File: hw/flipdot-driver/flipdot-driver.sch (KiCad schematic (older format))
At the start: 7 parts

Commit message: Last version before 74HC595.
Only partially routed.
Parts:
- removed D?: D_ALT, symbol Device:D_ALT
- removed Q?: Q_PMOS_GSD, symbol Device:Q_PMOS_GSD
- removed R?: R, symbol Device:R
- removed U?: STM32F103C8Tx, Package_QFP:LQFP-48_7x7mm_P0.5mm, symbol MCU_ST_STM32F1:STM32F103C8Tx
- removed U?: ULN2803A, symbol Transistor_Array:ULN2803A
- added C1: 100u, Capacitor_SMD:CP_Elec_6.3x5.3, symbol controller-cache:CP
- added C10: 10n, Capacitor_SMD:C_0603_1608Metric, symbol controller-cache:C
- added C11: 22u, Capacitor_SMD:C_0805_2012Metric, symbol controller-cache:C
- added C12, C13: 10p, Capacitor_SMD:C_0603_1608Metric, symbol controller-cache:C
- added C14, C15: 27p, Capacitor_SMD:C_0603_1608Metric, symbol controller-cache:C
- added C2, C3: 1u, Capacitor_SMD:C_0603_1608Metric, symbol controller-cache:C
- added C4: 220u, Capacitor_SMD:CP_Elec_10x10, symbol controller-cache:CP
- added C5, C6, C7, C8: 100n, Capacitor_SMD:C_0603_1608Metric, symbol controller-cache:C
- added C9: 10u, Capacitor_SMD:C_0805_2012Metric, symbol controller-cache:C
- added D1, D6: SK33, Diode_SMD:D_SMC, symbol controller-cache:D_Schottky
- added D3, D4, D5: LED, LED_THT:LED_D5.0mm_Horizontal_O6.35mm_Z9.0mm, symbol controller-cache:LED
- added DC1: XL6009, Package_TO_SOT_SMD:TO-263-5_TabPin3, symbol controller-cache:XL6009
- added F1: 200mA, Fuse:Fuse_1206_3216Metric, symbol Device:Polyfuse
- added F2: Polyfuse, Fuse:Fuse_1812_4532Metric, symbol Device:Polyfuse
- added J10: AUX_Power, Connector_Molex:Molex_KK-254_AE-6410-02A_1x02_P2.54mm_Vertical, symbol Connector_Generic:Conn_01x02
- added J11: GND, user:TestPoint_Plated_Hole_D1.6mm, symbol Connector:Conn_01x01_Female
- added J12: +VIN, user:TestPoint_Plated_Hole_D1.6mm, symbol Connector:Conn_01x01_Female
- added J2: NRF_CON, Connector_PinSocket_2.54mm:PinSocket_2x04_P2.54mm_Vertical, symbol Connector_Generic:Conn_02x04_Odd_Even
- added J3: Prog, Connector_Molex:Molex_KK-254_AE-6410-05A_1x05_P2.54mm_Vertical, symbol Connector_Generic:Conn_01x05
- added J4: I2C, Connector_Molex:Molex_KK-254_AE-6410-04A_1x04_P2.54mm_Vertical, symbol Connector_Generic:Conn_01x04
- added J5: USART, Connector_Molex:Molex_KK-254_AE-6410-05A_1x05_P2.54mm_Vertical, symbol Connector_Generic:Conn_01x05
- added J6: USB, Connector_Molex:Molex_KK-254_AE-6410-04A_1x04_P2.54mm_Vertical, symbol Connector_Generic:Conn_01x04
- added J7: USB_B_Micro, symbol Connector:USB_B_Micro
- added J8: RST, Connector_PinSocket_2.54mm:PinSocket_1x02_P2.54mm_Vertical, symbol Connector_Generic:Conn_01x02
- added J9: MAIN_Power, Connectors_Phoenix:PhoenixContact_MC-G_02x3.81mm_Angled, symbol Connector_Generic:Conn_01x02
- added L1: 33u, Inductor_SMD:L_12x12mm_H8mm, symbol controller-cache:L
- added Q1, Q10, Q11, Q12, Q13, Q14, Q2, Q3, Q4, Q5, Q6, Q7, Q8, Q9: MMBTA64, dboard_footprints:SOT23-3, symbol Device:Q_PNP_Darlington_BEC
- added Q15, Q16, Q17, Q18: Q_NMOS_GSD, Package_TO_SOT_SMD:SOT-23, symbol Device:Q_NMOS_GSD
- added R1, R13, R16, R27, R28, R29, R30, R31, R32, R33, R34: 12k, Resistor_SMD:R_0603_1608Metric, symbol Device:R
- added R14, R15: 22R, Resistor_SMD:R_0603_1608Metric, symbol Device:R
- added R2: 680R, Resistor_SMD:R_0603_1608Metric, symbol Device:R
- added R24: 1k5, Resistor_SMD:R_0603_1608Metric, symbol Device:R
- added R25, R3, R4: 330R, Resistor_SMD:R_0603_1608Metric, symbol Device:R
- added R26: 4k7, Resistor_SMD:R_0603_1608Metric, symbol Device:R
- added R35: 1M, Resistor_SMD:R_0603_1608Metric, symbol Device:R
- added R36: 1k5, Resistor_SMD:R_0603_1608Metric, symbol controller-cache:R
- added RN1, RN2, RN3, RN4: 10k, Resistor_SMD:R_Array_Convex_4x0603, symbol Device:R_Pack04
- added TP1: TestPoint, TestPoint:TestPoint_THTPad_2.5x2.5mm_Drill1.2mm, symbol Connector:TestPoint
- added U1: AT25xxx, Package_SO:SO-8_5.3x6.2mm_P1.27mm, symbol Memory_EEPROM:AT25xxx
- added U3: USBLC6-2SC6, Package_TO_SOT_SMD:SOT-23-6, symbol Power_Protection:USBLC6-2SC6
- added U4: AZ1117-3.3, Package_TO_SOT_SMD:SOT-223-3_TabPin2, symbol Regulator_Linear:AZ1117-3.3
- added U5: ULN2003A, Package_SO:SOIC-16_3.9x9.9mm_P1.27mm, symbol Transistor_Array:ULN2003A
- added U6: stm32_STM32F103C(8-B)Tx, Package_QFP:LQFP-48_7x7mm_P0.5mm, symbol STM32_converter-cache:stm32_STM32F103C(8-B)Tx
- added Y1: 32768, Crystal:Crystal_Round_D3.0mm_Vertical, symbol Device:Crystal
- added Y2: 8MHz/20pF, Crystal:Crystal_HC49-U_Vertical, symbol Device:Crystal
- J1: renamed from J?; value Conn_02x10_Top_Bottom -> DISPLAY; footprint (none) -> Connector_IDC:IDC-Header_2x10_P2.54mm_Vertical
- U2: renamed from U?; footprint (none) -> Package_SO:SOIC-16_3.9x9.9mm_P1.27mm
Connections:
- net labels added: +12V, +3V3, 24V_EN, FLASH_SS, I2C_SCL, I2C_SDA, LV_CLK, LV_DATA, LV_R1N, LV_R1P, LV_R2N, LV_R2P, LV_R3N, LV_R3P, LV_R4N, LV_R4P, LV_R5N, LV_R5P, LV_R6N, LV_R6P, LV_R7N, LV_R7P, LV_RET, LV_RST, NRF_CE, NRF_IRQ, NRF_SS, NRST, SPI_MISO, SPI_MOSI, SPI_SCK, SWCLK, SWDIO, USART_RX, USART_TX, USB1_N, USB1_P, USB_N, USB_P
- wire segments 28 -> 436
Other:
- moved on the sheet: J1, U2

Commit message: Added 74HC595 and AX5201
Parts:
- added C16: 470u, Capacitor_SMD:CP_Elec_6.3x5.3, symbol flipdot-driver-rescue:CP-controller-cache
- added C17: 100n, Capacitor_SMD:C_0603_1608Metric, symbol flipdot-driver-rescue:C-controller-cache
- added C18, C19: 470n, Capacitor_SMD:C_0603_1608Metric, symbol flipdot-driver-rescue:C-controller-cache
- added C20: 1u, Capacitor_SMD:C_0603_1608Metric, symbol flipdot-driver-rescue:C-controller-cache
- added C21: 220u, Capacitor_SMD:CP_Elec_10x10, symbol flipdot-driver-rescue:CP-controller-cache
- added D2: SK34, Diode_SMD:D_SMC, symbol flipdot-driver-rescue:D_Schottky-controller-cache
- added D7, D8: LED, LED_THT:LED_D5.0mm, symbol flipdot-driver-rescue:LED-controller-cache
- added L2: 68u, Inductor_SMD:L_12x12mm_H8mm, symbol flipdot-driver-rescue:L-controller-cache
- added R10, R5: 12k, Resistor_SMD:R_0603_1608Metric, symbol Device:R
- added R6: 30k, Resistor_SMD:R_0603_1608Metric, symbol Device:R
- added R7: 1.3k, Resistor_SMD:R_0603_1608Metric, symbol Device:R
- added R8, R9: 330R, Resistor_SMD:R_0603_1608Metric, symbol Device:R
- added TP2: TestPoint, TestPoint:TestPoint_THTPad_2.5x2.5mm_Drill1.2mm, symbol Connector:TestPoint
- added U7, U9: 74HC595, Package_SO:SOIC-16_3.9x9.9mm_P1.27mm, symbol 74xx:74HC595
- added U8: AX5201, Package_SO:HSOP-8-1EP_3.9x4.9mm_P1.27mm_EP2.41x3.1mm, symbol LCSC:AX5201
- C1, C4: symbol controller-cache:CP -> flipdot-driver-rescue:CP-controller-cache
- C10, C11, C12, C13, C14, C15, C2, C3, C5, C6, C7, C8, C9: symbol controller-cache:C -> flipdot-driver-rescue:C-controller-cache
- D1, D6: symbol controller-cache:D_Schottky -> flipdot-driver-rescue:D_Schottky-controller-cache
- D3, D4, D5: footprint LED_THT:LED_D5.0mm_Horizontal_O6.35mm_Z9.0mm -> LED_THT:LED_D5.0mm; symbol controller-cache:LED -> flipdot-driver-rescue:LED-controller-cache
- DC1: symbol controller-cache:XL6009 -> flipdot-driver-rescue:XL6009-controller-cache
- L1: symbol controller-cache:L -> flipdot-driver-rescue:L-controller-cache
- R36: symbol controller-cache:R -> flipdot-driver-rescue:R-controller-cache
- U6: symbol STM32_converter-cache:stm32_STM32F103C(8-B)Tx -> flipdot-driver-rescue:stm32_STM32F103C(8-B)Tx-STM32_converter-cache
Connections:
- net labels added: BOOT1, LED1, LED2, LV_RES, SR_CLK, SR_DATA1, SR_DATA2, SR_STROBE, ~SR_OE
- net labels removed: LV_R1N, LV_R1P, LV_R2N, LV_R2P, LV_R3N, LV_R3P, LV_R4N, LV_R4P, LV_R5N, LV_R5P, LV_R6N, LV_R6P, LV_R7N, LV_R7P
- wire segments 436 -> 521
- no-connect marks 0 -> 3
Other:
- moved on the sheet: F1, J1, J2, J3, J4, J5, Q1, Q2, Q3, Q4, Q5, Q6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

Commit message: Routed, with unused parts.
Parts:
- removed R14, R15: 22R, Resistor_SMD:R_0603_1608Metric, symbol Device:R
- added C22: 100n, Capacitor_SMD:C_0603_1608Metric, symbol flipdot-driver-rescue:C-controller-cache-flipdot-driver-rescue
- added R11, R12: 1k5, Resistor_SMD:R_0603_1608Metric, symbol controller-cache:R
- added RN5: 22R, Resistor_SMD:R_Array_Convex_2x0402, symbol Device:R_Pack02
- C1, C16, C4: symbol flipdot-driver-rescue:CP-controller-cache -> flipdot-driver-rescue:CP-controller-cache-flipdot-driver-rescue
- C10, C11, C12, C13, C14, C15, C17, C18, C19, C2, C20, C3, C5, C6, C7, C8, C9: symbol flipdot-driver-rescue:C-controller-cache -> flipdot-driver-rescue:C-controller-cache-flipdot-driver-rescue
- C21: value 220u -> 470u; symbol flipdot-driver-rescue:CP-controller-cache -> flipdot-driver-rescue:CP-controller-cache-flipdot-driver-rescue
- D1, D2, D6: symbol flipdot-driver-rescue:D_Schottky-controller-cache -> flipdot-driver-rescue:D_Schottky-controller-cache-flipdot-driver-rescue
- D3, D4, D5, D7, D8: footprint LED_THT:LED_D5.0mm -> LED_THT:LED_D3.0mm; symbol flipdot-driver-rescue:LED-controller-cache -> flipdot-driver-rescue:LED-controller-cache-flipdot-driver-rescue
- DC1: symbol flipdot-driver-rescue:XL6009-controller-cache -> flipdot-driver-rescue:XL6009-controller-cache-flipdot-driver-rescue
- J7: footprint (none) -> stm32_converter_footprints:USB_Micro-B
- L1, L2: symbol flipdot-driver-rescue:L-controller-cache -> flipdot-driver-rescue:L-controller-cache-flipdot-driver-rescue
- R36: symbol flipdot-driver-rescue:R-controller-cache -> flipdot-driver-rescue:R-controller-cache-flipdot-driver-rescue
- U6: symbol flipdot-driver-rescue:stm32_STM32F103C(8-B)Tx-STM32_converter-cache -> flipdot-driver-rescue:stm32_STM32F103C(8-B)Tx-STM32_converter-cache-flipdot-driver-rescue
- U8: symbol LCSC:AX5201 -> flipdot-driver-rescue:AX5201-LCSC
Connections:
- net labels added: USB2_N, USB2_P
- net labels removed: LV_RES
- wire segments 521 -> 529
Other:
- moved on the sheet: J4

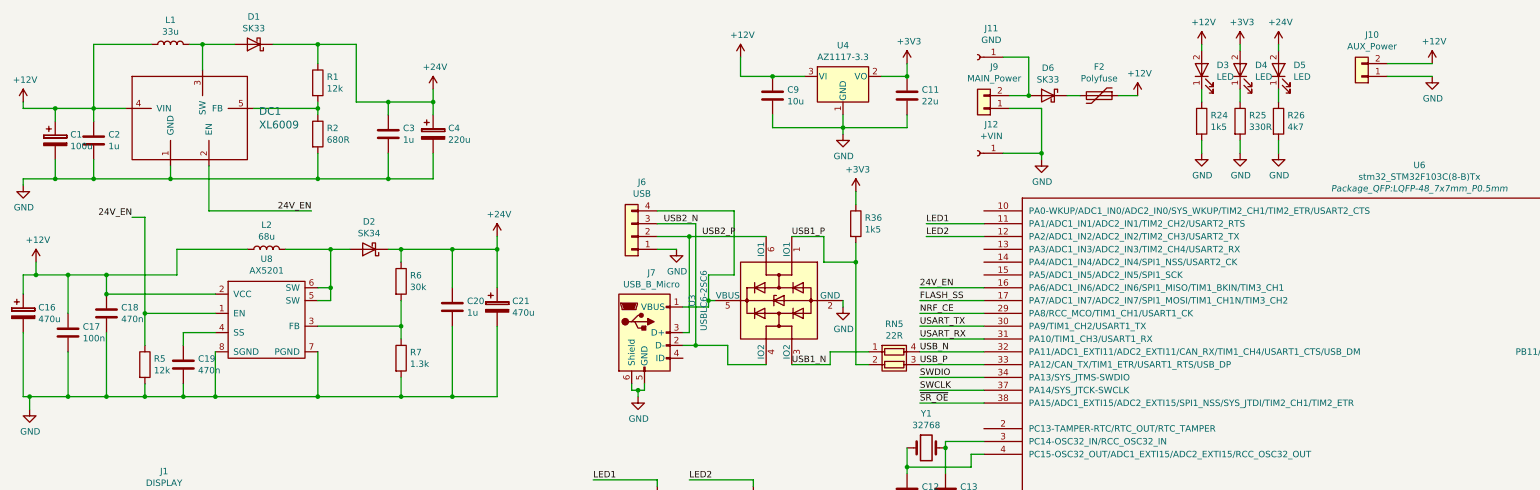
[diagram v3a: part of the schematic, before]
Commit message: Routed, without unused parts.
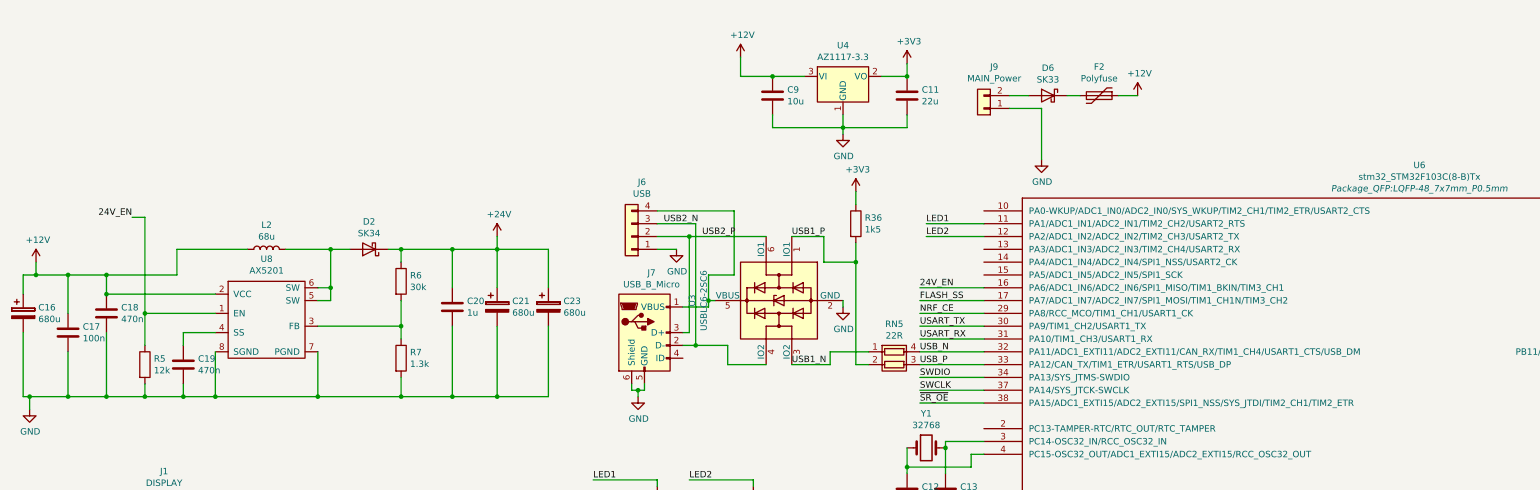
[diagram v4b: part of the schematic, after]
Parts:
- removed C1: 100u, Capacitor_SMD:CP_Elec_6.3x5.3, symbol flipdot-driver-rescue:CP-controller-cache-flipdot-driver-rescue
- removed C2, C3: 1u, Capacitor_SMD:C_0603_1608Metric, symbol flipdot-driver-rescue:C-controller-cache-flipdot-driver-rescue
- removed C4: 220u, Capacitor_SMD:CP_Elec_10x10, symbol flipdot-driver-rescue:CP-controller-cache-flipdot-driver-rescue
- removed D1: SK33, Diode_SMD:D_SMC, symbol flipdot-driver-rescue:D_Schottky-controller-cache-flipdot-driver-rescue
- removed D3, D4, D5: LED, LED_THT:LED_D3.0mm, symbol flipdot-driver-rescue:LED-controller-cache-flipdot-driver-rescue
- removed DC1: XL6009, Package_TO_SOT_SMD:TO-263-5_TabPin3, symbol flipdot-driver-rescue:XL6009-controller-cache-flipdot-driver-rescue
- removed J10: AUX_Power, Connector_Molex:Molex_KK-254_AE-6410-02A_1x02_P2.54mm_Vertical, symbol Connector_Generic:Conn_01x02
- removed J11: GND, user:TestPoint_Plated_Hole_D1.6mm, symbol Connector:Conn_01x01_Female
- removed J12: +VIN, user:TestPoint_Plated_Hole_D1.6mm, symbol Connector:Conn_01x01_Female
- removed L1: 33u, Inductor_SMD:L_12x12mm_H8mm, symbol flipdot-driver-rescue:L-controller-cache-flipdot-driver-rescue
- removed R1: 12k, Resistor_SMD:R_0603_1608Metric, symbol Device:R
- removed R2: 680R, Resistor_SMD:R_0603_1608Metric, symbol Device:R
- removed R24: 1k5, Resistor_SMD:R_0603_1608Metric, symbol Device:R
- removed R25: 330R, Resistor_SMD:R_0603_1608Metric, symbol Device:R
- removed R26: 4k7, Resistor_SMD:R_0603_1608Metric, symbol Device:R
- added C23: 680u, Capacitor_THT:CP_Radial_D10.0mm_P5.00mm, symbol flipdot-driver-rescue:CP-controller-cache-flipdot-driver-rescue
- C16: value 470u -> 680u; footprint Capacitor_SMD:CP_Elec_6.3x5.3 -> Capacitor_THT:CP_Radial_D10.0mm_P5.00mm
- C21: value 470u -> 680u; footprint Capacitor_SMD:CP_Elec_10x10 -> Capacitor_THT:CP_Radial_D10.0mm_P5.00mm
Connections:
- net +24V: now also C23.1
- net GND: now also C23.2
